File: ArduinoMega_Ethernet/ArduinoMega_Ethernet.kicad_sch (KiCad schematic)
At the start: 22 parts, among them J2 SD_DET_JUMP, J3 IMU_INT1_JUMP, J4 IMU_INT2_JUMP, J5 ETHER_INT_JUMP, J6 RTC_MFP_JUMP, SW1 RST_BTN, U1 ATmega2560-16A, Y1 16Mhz

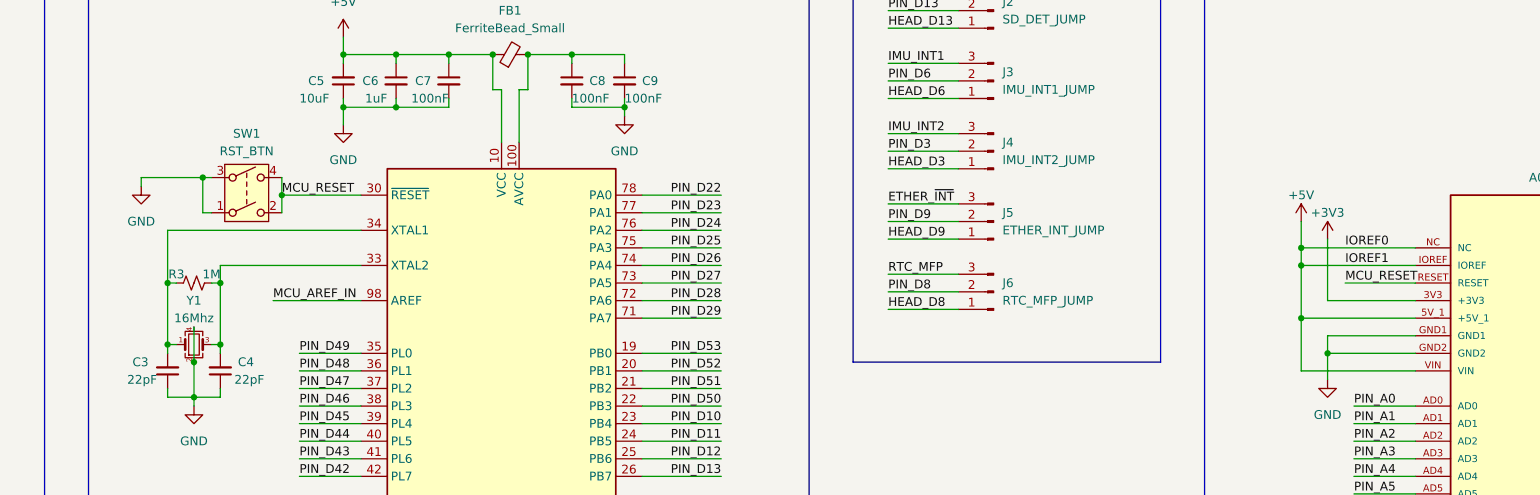
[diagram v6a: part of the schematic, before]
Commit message: fix VIN pin
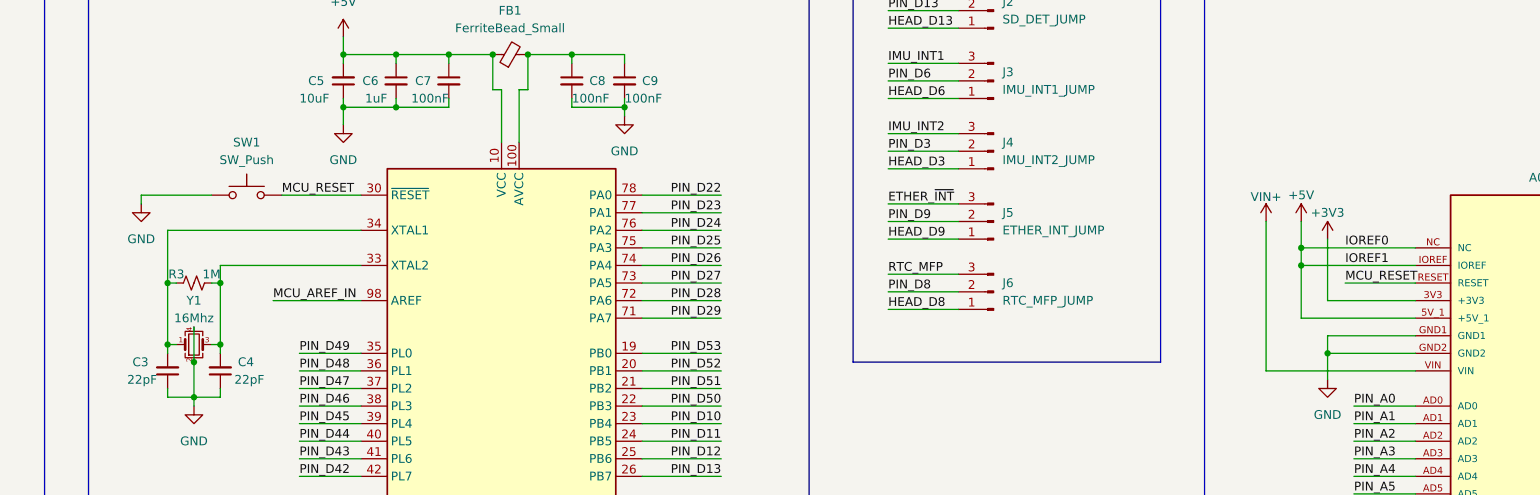
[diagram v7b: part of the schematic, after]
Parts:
- removed SW1: RST_BTN, Button_Switch_SMD:SW_SPST_PTS645, symbol Switch:SW_DPST
- added SW1: SW_Push, Button_Switch_SMD:SW_Push_SPST_NO_Alps_SKRK, symbol Switch:SW_Push
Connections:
- net +5V: no longer A1.VIN
- net GND: now also SW1.1
- net MCU_RESET: now also SW1.2
- new net VIN+: A1.VIN
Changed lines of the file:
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@@
 	)
 	(junction
-		(at 142.24 74.93)
-		(diameter 0)
-		(color 0 0 0 0)
-	)
-	(junction
 		(at 137.16 90.17)
 		(diameter 0)
@@
 	)
 	(junction
-		(at 300.99 95.25)
-		(diameter 0)
-		(color 0 0 0 0)
-	)
-	(junction
 		(at 177.8 57.15)
 		(diameter 0)
@@
 	)
 	(junction
-		(at 153.67 77.47)
-		(diameter 0)
-		(color 0 0 0 0)
-	)
-	(junction
 		(at 300.99 85.09)
 		(diameter 0)
@@
 	(wire
 		(pts
-			(xy 143.51 80.01) (xy 142.24 80.01)
-		)
-		(stroke
-			(width 0)
-			(type default)
-		)
-	)
-	(wire
-		(pts
 			(xy 367.03 148.59) (xy 358.14 148.59)
 		)
@@
 	(wire
 		(pts
-			(xy 142.24 80.01) (xy 142.24 74.93)
-		)
-		(stroke
-			(width 0)
-			(type default)
-		)
-	)
-	(wire
-		(pts
 			(xy 317.5 158.75) (xy 308.61 158.75)
 		)
@@
 	(wire
 		(pts
+			(xy 295.91 102.87) (xy 317.5 102.87)
+		)
+		(stroke
+			(width 0)
+			(type default)
+		)
+	)
+	(wire
+		(pts
 			(xy 205.74 176.53) (xy 217.17 176.53)
 		)
@@
 	(wire
 		(pts
-			(xy 153.67 74.93) (xy 153.67 77.47)
-		)
-		(stroke
-			(width 0)
-			(type default)
-		)
-	)
-	(wire
-		(pts
 			(xy 300.99 85.09) (xy 300.99 87.63)
 		)
@@
 	(wire
 		(pts
-			(xy 143.51 74.93) (xy 142.24 74.93)
+			(xy 133.35 77.47) (xy 143.51 77.47)
 		)
 		(stroke
@@
 	(wire
 		(pts
-			(xy 300.99 102.87) (xy 317.5 102.87)
-		)
-		(stroke
-			(width 0)
-			(type default)
-		)
-	)
-	(wire
-		(pts
 			(xy 367.03 118.11) (xy 358.14 118.11)
 		)
@@
 	(wire
 		(pts
-			(xy 142.24 74.93) (xy 133.35 74.93)
-		)
-		(stroke
-			(width 0)
-			(type default)
-		)
-	)
-	(wire
-		(pts
 			(xy 367.03 156.21) (xy 358.14 156.21)
 		)
@@
 	(wire
 		(pts
-			(xy 133.35 74.93) (xy 133.35 76.2)
+			(xy 133.35 77.47) (xy 133.35 78.74)
 		)
 		(stroke
@@
 	(wire
 		(pts
-			(xy 153.67 77.47) (xy 153.67 80.01)
-		)
-		(stroke
-			(width 0)
-			(type default)
-		)
-	)
-	(wire
-		(pts
 			(xy 241.3 71.12) (xy 251.46 71.12)
 		)
@@
 	(wire
 		(pts
+			(xy 295.91 81.28) (xy 295.91 102.87)
+		)
+		(stroke
+			(width 0)
+			(type default)
+		)
+	)
+	(wire
+		(pts
 			(xy 367.03 161.29) (xy 358.14 161.29)
 		)
@@
 	(wire
 		(pts
-			(xy 300.99 102.87) (xy 300.99 95.25)
-		)
-		(stroke
-			(width 0)
-			(type default)
-		)
-	)
-	(wire
-		(pts
 			(xy 156.21 168.91) (xy 165.1 168.91)
 		)
@@
 	)
 	(symbol
-		(lib_id "Switch:SW_DPST")
-		(at 148.59 77.47 0)
-		(unit 1)
-		(exclude_from_sim no)
-		(in_bom yes)
-		(on_board yes)
-		(dnp no)
-		(fields_autoplaced yes)
-		(property "Reference" "SW1"
-			(at 148.59 68.58 0)
-			(effects
-				(font
-					(size 1.27 1.27)
-				)
-			)
-		)
-		(property "Value" "RST_BTN"
-			(at 148.59 71.12 0)
-			(effects
-				(font
-					(size 1.27 1.27)
-				)
-			)
-		)
-		(property "Footprint" "Button_Switch_SMD:SW_SPST_PTS645"
-			(at 148.59 77.47 0)
-			(effects
-				(font
-					(size 1.27 1.27)
-				)
-				(hide yes)
-			)
-		)
-		(property "Datasheet" "~"
-			(at 148.59 77.47 0)
-			(effects
-				(font
-					(size 1.27 1.27)
-				)
-				(hide yes)
-			)
-		)
-		(property "Description" "Double Pole Single Throw (DPST) Switch"
-			(at 148.59 77.47 0)
-			(effects
-				(font
-					(size 1.27 1.27)
-				)
-				(hide yes)
-			)
-		)
-		(pin "1"
-		)
-		(pin "2"
-		)
-		(pin "3"
-		)
-		(pin "4"
-		)
-		(instances
-			(project ""
-				(path "/e63e39d7-6ac0-4ffd-8aa3-1841a4541b55"
-					(reference "SW1")
-					(unit 1)
-				)
-			)
-		)
-	)
-	(symbol
 		(lib_id "power:GND")
 		(at 203.2 66.04 0)
@@
 	)
 	(symbol
+		(lib_id "Switch:SW_Push")
+		(at 148.59 77.47 0)
+		(unit 1)
+		(exclude_from_sim no)
+		(in_bom yes)
+		(on_board yes)
+		(dnp no)
+		(fields_autoplaced yes)
+		(property "Reference" "SW1"
+			(at 148.59 69.85 0)
+			(effects
+				(font
+					(size 1.27 1.27)
+				)
+			)
+		)
+		(property "Value" "SW_Push"
+			(at 148.59 72.39 0)
+			(effects
+				(font
+					(size 1.27 1.27)
+				)
+			)
+		)
+		(property "Footprint" "Button_Switch_SMD:SW_Push_SPST_NO_Alps_SKRK"
+			(at 148.59 72.39 0)
+			(effects
+				(font
+					(size 1.27 1.27)
+				)
+				(hide yes)
+			)
+		)
+		(property "Datasheet" "~"
+			(at 148.59 72.39 0)
+			(effects
+				(font
+					(size 1.27 1.27)
+				)
+				(hide yes)
+			)
+		)
+		(property "Description" "Push button switch, generic, two pins"
+			(at 148.59 77.47 0)
+			(effects
+				(font
+					(size 1.27 1.27)
+				)
+				(hide yes)
+			)
+		)
+		(pin "2"
+		)
+		(pin "1"
+		)
+		(instances
+			(project ""
+				(path "/e63e39d7-6ac0-4ffd-8aa3-1841a4541b55"
+					(reference "SW1")
+					(unit 1)
+				)
+			)
+		)
+	)
+	(symbol
 		(lib_id "A000067:A000067")
 		(at 337.82 138.43 0)
@@
 	(symbol
 		(lib_id "power:GND")
-		(at 133.35 76.2 0)
+		(at 133.35 78.74 0)
 		(unit 1)
 		(exclude_from_sim no)
@@
 		(fields_autoplaced yes)
 		(property "Reference" "#PWR0105"
-			(at 133.35 82.55 0)
+			(at 133.35 85.09 0)
 			(effects
 				(font
@@
 		)
 		(property "Value" "GND"
-			(at 133.35 81.28 0)
+			(at 133.35 83.82 0)
 			(effects
 				(font
@@
 		)
 		(property "Footprint" ""
-			(at 133.35 76.2 0)
+			(at 133.35 78.74 0)
 			(effects
 				(font
@@
 		)
 		(property "Datasheet" ""
-			(at 133.35 76.2 0)
+			(at 133.35 78.74 0)
 			(effects
 				(font
@@
 		)
 		(property "Description" ""
-			(at 133.35 76.2 0)
+			(at 133.35 78.74 0)
 			(effects
 				(font
@@
 					(unit 1)
 				)
+			)
+		)
+	)
+	(symbol
+		(lib_id "power:+12V")
+		(at 295.91 81.28 0)
+		(unit 1)
+		(exclude_from_sim no)
+		(in_bom yes)
+		(on_board yes)
+		(dnp no)
+		(property "Reference" "#PWR04"
+			(at 295.91 85.09 0)
+			(effects
+				(font
+					(size 1.27 1.27)
+				)
+				(hide yes)
+			)
+		)
+		(property "Value" "VIN+"
+			(at 295.91 77.724 0)
+			(effects
+				(font
+					(size 1.27 1.27)
+				)
+			)
+		)
+		(property "Footprint" ""
+			(at 295.91 81.28 0)
+			(effects
+				(font
+					(size 1.27 1.27)
+				)
+				(hide yes)
+			)
+		)
+		(property "Datasheet" ""
+			(at 295.91 81.28 0)
+			(effects
+				(font
+					(size 1.27 1.27)
+				)
+				(hide yes)
+			)
+		)
+		(property "Description" "Power symbol creates a global label with name \"+12V\""
+			(at 295.91 81.28 0)
+			(effects
+				(font
+					(size 1.27 1.27)
+				)
+				(hide yes)
+			)
+		)
+		(pin "1"
+		)
+		(instances
+			(project ""
+				(path "/e63e39d7-6ac0-4ffd-8aa3-1841a4541b55"
+					(reference "#PWR04")
+					(unit 1)
+				)

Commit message: finished BOM and component sizing
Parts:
- C1: value TBD -> 100nF
- C2: value TBD -> 22pF
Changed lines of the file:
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@@
 		(dnp no)
 		(property "Reference" "C1"
-			(at 85.09 60.96 90)
+			(at 85.09 60.198 90)
 			(effects
 				(font
@@
 			)
 		)
-		(property "Value" "TBD"
-			(at 78.74 60.96 90)
+		(property "Value" "100nF"
+			(at 76.962 60.198 90)
 			(effects
 				(font
@@
 			)
 		)
-		(property "Value" "TBD"
+		(property "Value" "22pF"
 			(at 90.17 68.58 0)
 			(effects
